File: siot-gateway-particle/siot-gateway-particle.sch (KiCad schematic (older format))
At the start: 0 parts

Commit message: 1st pass of gw finished
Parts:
- added C1: 4.7uF_100V, Capacitor_SMD:C_2220_5650Metric, symbol bec-passive:4.7uF_100V
- added C2: 100pF, Capacitor_SMD:C_0603_1608Metric, symbol Device:C
- added C3, C4: 100uF_6.3V, Capacitor_SMD:C_1210_3225Metric, symbol bec-passive:100uF_6.3V
- added C5, C6: 0.1uF, Capacitor_SMD:C_0603_1608Metric, symbol Device:C
- added H1, H2, H3, H4: MountingHole, MountingHole:MountingHole_3.5mm, symbol Mechanical:MountingHole
- added J1, J2: xConnect, BEC:xConnect, symbol bec-connector:xConnect
- added L1: 33uH_2.5A_84mOhm, BEC:CDRH105R, symbol bec-passive:33uH_2.5A_84mOhm
- added R1: 220K, Resistor_SMD:R_0603_1608Metric, symbol bec-passive:R_0603
- added U1: Particle_Mesh, feather, symbol bec-particle:Particle_Mesh
- added U2: LTC3630, BEC:MSOP-12-16-1EP_3x4mm_P0.5mm_EP1.65x2.85mm_ThermalVias, symbol bec-power:LTC3630
- added U3, U4: DS2483R, Package_TO_SOT_SMD:TSOT-23-6, symbol bec-interface:DS2483R
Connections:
- net labels added: +24V, +3V3, +5V, GND, SCL, SDA
- wire segments 0 -> 80
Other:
- note added: "Downstream\nConnector\n"
- note added: "Upstream\nConnector\n"

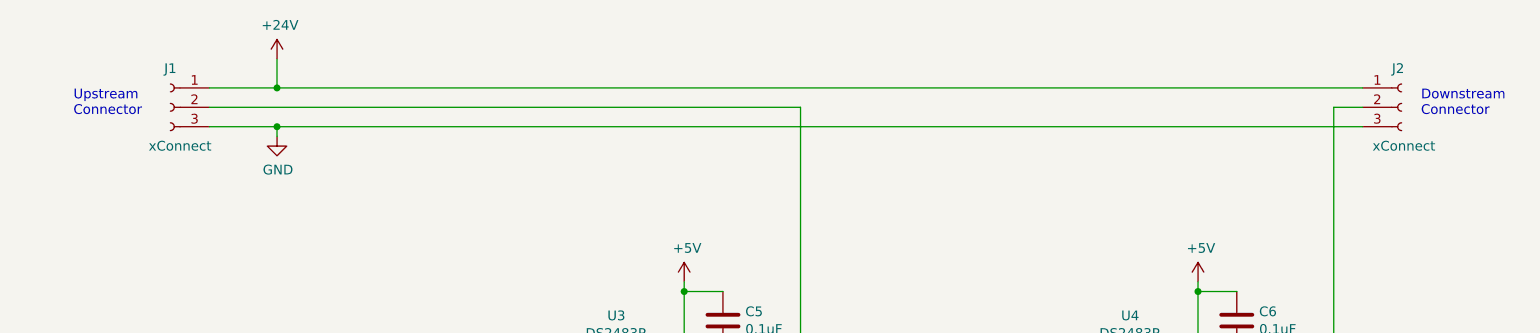
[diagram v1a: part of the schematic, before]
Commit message: work on SMD xConnect connections
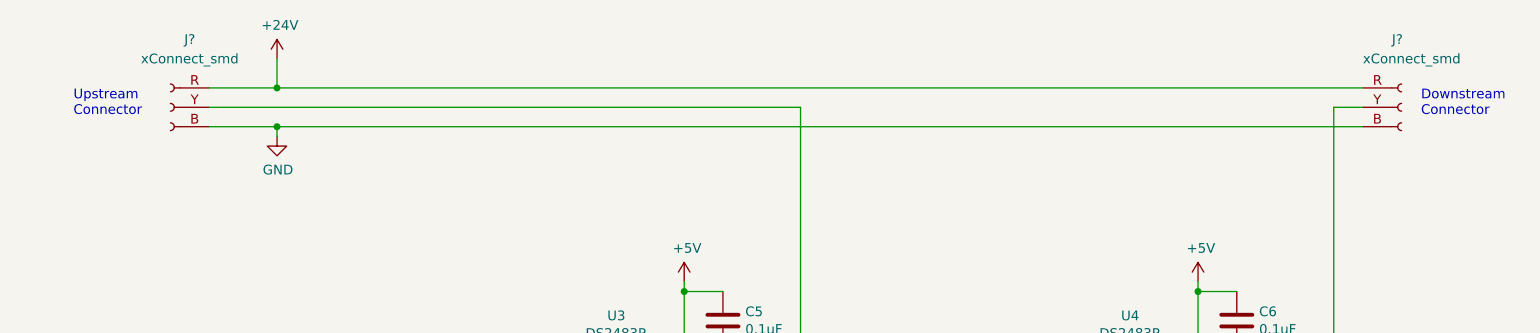
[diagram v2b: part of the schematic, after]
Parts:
- removed J1, J2: xConnect, BEC:xConnect, symbol bec-connector:xConnect
- added J? (x2): xConnect_smd, BEC:xConnect_smd, symbol bec-connector:xConnect_smd
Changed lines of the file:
@@
 EESchema Schematic File Version 4
 LIBS:siot-gateway-particle-cache
-EELAYER 30 0
+EELAYER 29 0
 EELAYER END
 $Descr USLetter 11000 8500
@@
 $EndComp
 $Comp
-L bec-connector:xConnect J1
-U 1 1 5D5E6D90
-P 1750 1250
-F 0 "J1" H 1750 1450 50  0000 C CNN
-F 1 "xConnect" H 1700 1050 50  0000 C CNN
-F 2 "BEC:xConnect" H 1700 1000 50  0001 C CNN
-F 3 "~" H 1750 1250 50  0001 C CNN
-	1    1750 1250
-	-1   0    0    -1
-$EndComp
-$Comp
-L bec-connector:xConnect J2
-U 1 1 5D5E6F22
-P 8100 1250
-F 0 "J2" H 8050 1450 50  0000 L CNN
-F 1 "xConnect" H 7950 1050 50  0000 L CNN
-F 2 "BEC:xConnect" H 8050 1000 50  0001 C CNN
-F 3 "~" H 8100 1250 50  0001 C CNN
-	1    8100 1250
-	1    0    0    -1
-$EndComp
-$Comp
 L power:+3V3 #PWR0101
 U 1 1 5D5F7647
@@
 Wire Wire Line
 	7550 4450 7550 4350
+$Comp
+L bec-connector:xConnect_smd J?
+U 1 1 5D622C61
+P 1750 1250
+F 0 "J?" H 1650 1600 50  0000 C CNN
+F 1 "xConnect_smd" H 1650 1500 50  0000 C CNN
+F 2 "BEC:xConnect_smd" H 1700 1000 50  0001 C CNN
+F 3 "~" H 1750 1250 50  0001 C CNN
+	1    1750 1250
+	-1   0    0    -1
+$EndComp
+$Comp
+L bec-connector:xConnect_smd J?
+U 1 1 5D626702
+P 8100 1250
+F 0 "J?" H 8050 1600 50  0000 L CNN
+F 1 "xConnect_smd" H 7900 1500 50  0000 L CNN
+F 2 "BEC:xConnect_smd" H 8050 1000 50  0001 C CNN
+F 3 "~" H 8100 1250 50  0001 C CNN
+	1    8100 1250
+	1    0    0    -1
+$EndComp
 $EndSCHEMATC

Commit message: updates
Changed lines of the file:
@@
 EESchema Schematic File Version 4
 LIBS:siot-gateway-particle-cache
-EELAYER 29 0
+EELAYER 30 0
 EELAYER END
 $Descr USLetter 11000 8500
@@
 	3200 6150 3200 6200
 Connection ~ 3200 6150
-$Comp
-L power:+5V #PWR0112
-U 1 1 5D630671
-P 4400 2150
-F 0 "#PWR0112" H 4400 2000 50  0001 C CNN
-F 1 "+5V" H 4415 2323 50  0000 C CNN
-F 2 "" H 4400 2150 50  0001 C CNN
-F 3 "" H 4400 2150 50  0001 C CNN
-	1    4400 2150
-	1    0    0    -1
-$EndComp
 Wire Wire Line
 	4400 2150 4400 2200
@@
 Wire Wire Line
 	4600 2500 4600 2550
-$Comp
-L power:+5V #PWR0114
-U 1 1 5D63CC06
-P 7050 2150
-F 0 "#PWR0114" H 7050 2000 50  0001 C CNN
-F 1 "+5V" H 7065 2323 50  0000 C CNN
-F 2 "" H 7050 2150 50  0001 C CNN
-F 3 "" H 7050 2150 50  0001 C CNN
-	1    7050 2150
-	1    0    0    -1
-$EndComp
 $Comp
 L Device:C C6
@@
 	1    0    0    -1
 $EndComp
+$Comp
+L power:+3V3 #PWR?
+U 1 1 5D61D330
+P 4400 2150
+F 0 "#PWR?" H 4400 2000 50  0001 C CNN
+F 1 "+3V3" H 4415 2323 50  0000 C CNN
+F 2 "" H 4400 2150 50  0001 C CNN
+F 3 "" H 4400 2150 50  0001 C CNN
+	1    4400 2150
+	1    0    0    -1
+$EndComp
+$Comp
+L power:+3V3 #PWR?
+U 1 1 5D61D77B
+P 7050 2150
+F 0 "#PWR?" H 7050 2000 50  0001 C CNN
+F 1 "+3V3" H 7065 2323 50  0000 C CNN
+F 2 "" H 7050 2150 50  0001 C CNN
+F 3 "" H 7050 2150 50  0001 C CNN
+	1    7050 2150
+	1    0    0    -1
+$EndComp

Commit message: design updates
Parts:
- added D1: D_1A_30V_310mV, Diode_SMD:D_PowerDI-123, symbol bec-passive:D_1A_30V_310mV
- added D2, D3: SMBJ5.0A, Diode_SMD:D_SMB, symbol bec-passive:SMBJ5.0A
- added J3: Conn_01x03, Connector_PinHeader_2.54mm:PinHeader_1x03_P2.54mm_Vertical, symbol Connector_Generic:Conn_01x03
- added R2, R3: 150, Resistor_SMD:R_0603_1608Metric, symbol Device:R_US
- U3, U4: MPN (none) -> DS2483R+T; Manufacturer (none) -> Maxim Integrated
- gave numbers to parts that had none: 2
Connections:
- net labels added: +BATT
- wire segments 80 -> 101
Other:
- note added: "5V supply is designed to run from 5V to 24V."
- note added: "Connector for LEDs"
- note added: "NP: The reverse current of this diode is likely too high\nand will float charge the battery so don't install for now\n -- this is more of a placeholder at this point."
- moved on the sheet: C1, C2, C3, C4, J1, J2, L1, R1, U2

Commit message: GW tweaks
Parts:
- removed D1: D_1A_30V_310mV, Diode_SMD:D_PowerDI-123, symbol bec-passive:D_1A_30V_310mV
- added R? (x2): 4.7K, Resistor_SMD:R_0603_1608Metric, symbol Device:R_US
- U2: MPN (none) -> LTC3630EMSE#PBF; Manufacturer (none) -> Analog Devices
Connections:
- wire segments 101 -> 104
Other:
- note removed: "NP: The reverse current of this diode is likely too high\nand will float charge the battery so don't install for now\n -- this is more of a placeholder at this point."
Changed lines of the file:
@@
 Wire Wire Line
 	5400 4150 5400 4750
-Wire Wire Line
-	7400 5250 7900 5250
-Wire Wire Line
-	7400 5350 7900 5350
 Text Label 7550 5250 0    50   ~ 0
 SCL
@@
 Wire Wire Line
 	3600 4350 3600 2550
-$Comp
-L bec-power:LTC3630 U2
-U 1 1 5D5F3C86
-P 2150 6200
-F 0 "U2" H 2125 6725 50  0000 C CNN
-F 1 "LTC3630" H 2125 6634 50  0000 C CNN
-F 2 "BEC:MSOP-12-16-1EP_3x4mm_P0.5mm_EP1.65x2.85mm_ThermalVias" H 400 6650 50  0001 C CNN
-F 3 "" H 400 6650 50  0001 C CNN
-	1    2150 6200
-	1    0    0    -1
-$EndComp
 $Comp
 L power:+24V #PWR0102
@@
 $EndComp
 $Comp
-L power:+3V3 #PWR0112
-U 1 1 5D61D330
-P 4400 2150
-F 0 "#PWR0112" H 4400 2000 50  0001 C CNN
-F 1 "+3V3" H 4415 2323 50  0000 C CNN
-F 2 "" H 4400 2150 50  0001 C CNN
-F 3 "" H 4400 2150 50  0001 C CNN
-	1    4400 2150
-	1    0    0    -1
-$EndComp
-$Comp
-L power:+3V3 #PWR0114
-U 1 1 5D61D77B
-P 7050 2150
-F 0 "#PWR0114" H 7050 2000 50  0001 C CNN
-F 1 "+3V3" H 7065 2323 50  0000 C CNN
-F 2 "" H 7050 2150 50  0001 C CNN
-F 3 "" H 7050 2150 50  0001 C CNN
-	1    7050 2150
-	1    0    0    -1
-$EndComp
-$Comp
 L power:+BATT #PWR0119
 U 1 1 5D65A596
@@
 Wire Wire Line
 	7750 2800 7750 1850
-Wire Wire Line
-	2850 1450 7900 1450
-Wire Wire Line
-	2300 1450 2850 1450
-Connection ~ 2850 1450
-Wire Wire Line
-	2850 1300 2850 1450
-Wire Wire Line
-	2850 850  2850 1000
-$Comp
-L bec-passive:D_1A_30V_310mV D1
-U 1 1 5D66498A
-P 2850 1150
-F 0 "D1" V 2896 1071 50  0000 R CNN
-F 1 "D_1A_30V_310mV" V 2805 1071 50  0000 R CNN
-F 2 "Diode_SMD:D_PowerDI-123" H 2800 800 50  0001 C CNN
-F 3 "https://www.diodes.com/assets/Datasheets/ds30492.pdf" H 2850 1150 50  0001 C CNN
-F 4 "DFLS130L-7" H 2850 950 50  0001 C CNN "MPN"
-F 5 "Diodes Incorporated" H 2850 900 50  0001 C CNN "Manufacturer"
-	1    2850 1150
-	0    -1   -1   0
-$EndComp
-$Comp
-L power:+BATT #PWR0120
-U 1 1 5D664010
-P 2850 850
-F 0 "#PWR0120" H 2850 700 50  0001 C CNN
-F 1 "+BATT" H 2865 1023 50  0000 C CNN
-F 2 "" H 2850 850 50  0001 C CNN
-F 3 "" H 2850 850 50  0001 C CNN
-	1    2850 850
-	1    0    0    -1
-$EndComp
-Text Notes 3100 1000 0    50   ~ 0
-NP: The reverse current of this diode is likely too high\nand will float charge the battery so don't install for now\n -- this is more of a placeholder at this point.
 Text Notes 1650 5550 0    50   ~ 0
 5V supply is designed to run from 5V to 24V.
@@
 Text Notes 3550 4800 0    50   ~ 0
 Connector for LEDs
+Wire Wire Line
+	2300 1450 7900 1450
+$Comp
+L power:+5V #PWR?
+U 1 1 5DA93BC5
+P 4400 2150
+F 0 "#PWR?" H 4400 2000 50  0001 C CNN
+F 1 "+5V" H 4415 2323 50  0000 C CNN
+F 2 "" H 4400 2150 50  0001 C CNN
+F 3 "" H 4400 2150 50  0001 C CNN
+	1    4400 2150
+	1    0    0    -1
+$EndComp
+$Comp
+L power:+5V #PWR?
+U 1 1 5DA94452
+P 7050 2150
+F 0 "#PWR?" H 7050 2000 50  0001 C CNN
+F 1 "+5V" H 7065 2323 50  0000 C CNN
+F 2 "" H 7050 2150 50  0001 C CNN
+F 3 "" H 7050 2150 50  0001 C CNN
+	1    7050 2150
+	1    0    0    -1
+$EndComp
+$Comp
+L Device:R_US R?
+U 1 1 5DA94EC2
+P 8100 4900
+F 0 "R?" V 8200 4900 50  0000 C CNN
+F 1 "4.7K" V 7986 4900 50  0000 C CNN
+F 2 "Resistor_SMD:R_0603_1608Metric" V 8140 4890 50  0001 C CNN
+F 3 "~" H 8100 4900 50  0001 C CNN
+	1    8100 4900
+	-1   0    0    1
+$EndComp
+$Comp
+L Device:R_US R?
+U 1 1 5DA957A7
+P 8450 4900
+F 0 "R?" V 8550 4900 50  0000 C CNN
+F 1 "4.7K" V 8336 4900 50  0000 C CNN
+F 2 "Resistor_SMD:R_0603_1608Metric" V 8490 4890 50  0001 C CNN
+F 3 "~" H 8450 4900 50  0001 C CNN
+	1    8450 4900
+	-1   0    0    1
+$EndComp
+$Comp
+L power:+3V3 #PWR?
+U 1 1 5DA95A0F
+P 8100 4650
+F 0 "#PWR?" H 8100 4500 50  0001 C CNN
+F 1 "+3V3" H 8115 4823 50  0000 C CNN
+F 2 "" H 8100 4650 50  0001 C CNN
+F 3 "" H 8100 4650 50  0001 C CNN
+	1    8100 4650
+	1    0    0    -1
+$EndComp
+Wire Wire Line
+	8100 4650 8100 4700
+Wire Wire Line
+	8100 4700 8450 4700
+Wire Wire Line
+	8450 4700 8450 4750
+Connection ~ 8100 4700
+Wire Wire Line
+	8100 4700 8100 4750
+Wire Wire Line
+	8100 5050 8100 5250
+Wire Wire Line
+	7400 5250 8100 5250
+Wire Wire Line
+	8450 5050 8450 5350
+Wire Wire Line
+	7400 5350 8450 5350
+$Comp
+L bec-power:LTC3630 U2
+U 1 1 5D5F3C86
+P 2150 6200
+F 0 "U2" H 2125 6725 50  0000 C CNN
+F 1 "LTC3630" H 2125 6634 50  0000 C CNN
+F 2 "BEC:MSOP-12-16-1EP_3x4mm_P0.5mm_EP1.65x2.85mm_ThermalVias" H 400 6650 50  0001 C CNN
+F 3 "https://www.analog.com/media/en/technical-documentation/data-sheets/3630fd.pdf" H 400 6650 50  0001 C CNN
+F 4 "LTC3630EMSE#PBF" H 2150 6200 50  0001 C CNN "MPN"
+F 5 "Analog Devices" H 2150 6200 50  0001 C CNN "Manufacturer"
+	1    2150 6200
+	1    0    0    -1
+$EndComp
 $EndSCHEMATC

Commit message: start of gateway changes
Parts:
- gave numbers to parts that had none: 2
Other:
- note added: "5V,500mA supply is designed to run from 5V to 24V."
- note added: "Boron: Operating current (uC on, radio on): 100-200mA\nBoron: Peak current LTE: 120-490mA"
- note removed: "5V supply is designed to run from 5V to 24V."
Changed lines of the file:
@@
 EESchema Schematic File Version 4
-LIBS:siot-gateway-particle-cache
 EELAYER 30 0
 EELAYER END
@@
 	7750 2800 7750 1850
 Text Notes 1650 5550 0    50   ~ 0
-5V supply is designed to run from 5V to 24V.
+5V,500mA supply is designed to run from 5V to 24V.
 $Comp
 L bec-passive:SMBJ5.0A D2
@@
 	2300 1450 7900 1450
 $Comp
-L power:+5V #PWR?
+L power:+5V #PWR0112
 U 1 1 5DA93BC5
 P 4400 2150
-F 0 "#PWR?" H 4400 2000 50  0001 C CNN
+F 0 "#PWR0112" H 4400 2000 50  0001 C CNN
 F 1 "+5V" H 4415 2323 50  0000 C CNN
 F 2 "" H 4400 2150 50  0001 C CNN
@@
 $EndComp
 $Comp
-L power:+5V #PWR?
+L power:+5V #PWR0114
 U 1 1 5DA94452
 P 7050 2150
-F 0 "#PWR?" H 7050 2000 50  0001 C CNN
+F 0 "#PWR0114" H 7050 2000 50  0001 C CNN
 F 1 "+5V" H 7065 2323 50  0000 C CNN
 F 2 "" H 7050 2150 50  0001 C CNN
@@
 $EndComp
 $Comp
-L Device:R_US R?
+L Device:R_US R4
 U 1 1 5DA94EC2
 P 8100 4900
-F 0 "R?" V 8200 4900 50  0000 C CNN
+F 0 "R4" V 8200 4900 50  0000 C CNN
 F 1 "4.7K" V 7986 4900 50  0000 C CNN
 F 2 "Resistor_SMD:R_0603_1608Metric" V 8140 4890 50  0001 C CNN
@@
 $EndComp
 $Comp
-L Device:R_US R?
+L Device:R_US R5
 U 1 1 5DA957A7
 P 8450 4900
-F 0 "R?" V 8550 4900 50  0000 C CNN
+F 0 "R5" V 8550 4900 50  0000 C CNN
 F 1 "4.7K" V 8336 4900 50  0000 C CNN
 F 2 "Resistor_SMD:R_0603_1608Metric" V 8490 4890 50  0001 C CNN
@@
 $EndComp
 $Comp
-L power:+3V3 #PWR?
+L power:+3V3 #PWR0120
 U 1 1 5DA95A0F
 P 8100 4650
-F 0 "#PWR?" H 8100 4500 50  0001 C CNN
+F 0 "#PWR0120" H 8100 4500 50  0001 C CNN
 F 1 "+3V3" H 8115 4823 50  0000 C CNN
 F 2 "" H 8100 4650 50  0001 C CNN
@@
 	1    0    0    -1
 $EndComp
+Text Notes 5050 6150 0    50   ~ 0
+Boron: Operating current (uC on, radio on): 100-200mA\nBoron: Peak current LTE: 120-490mA
 $EndSCHEMATC
